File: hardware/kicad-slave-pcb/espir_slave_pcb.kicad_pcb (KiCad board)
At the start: 2 copper layers, 52 x 47 mm, 38 parts, among them Q2 AO3400A, Q4 AO3401A, SW1 RESET, SW2 BOOT, SW3 SS12D07VG6, U2 IR333C, U3 IR333C, U5 ESP32-C6-MINI-1, U6 AP2112K-3.3, U7 LiPo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

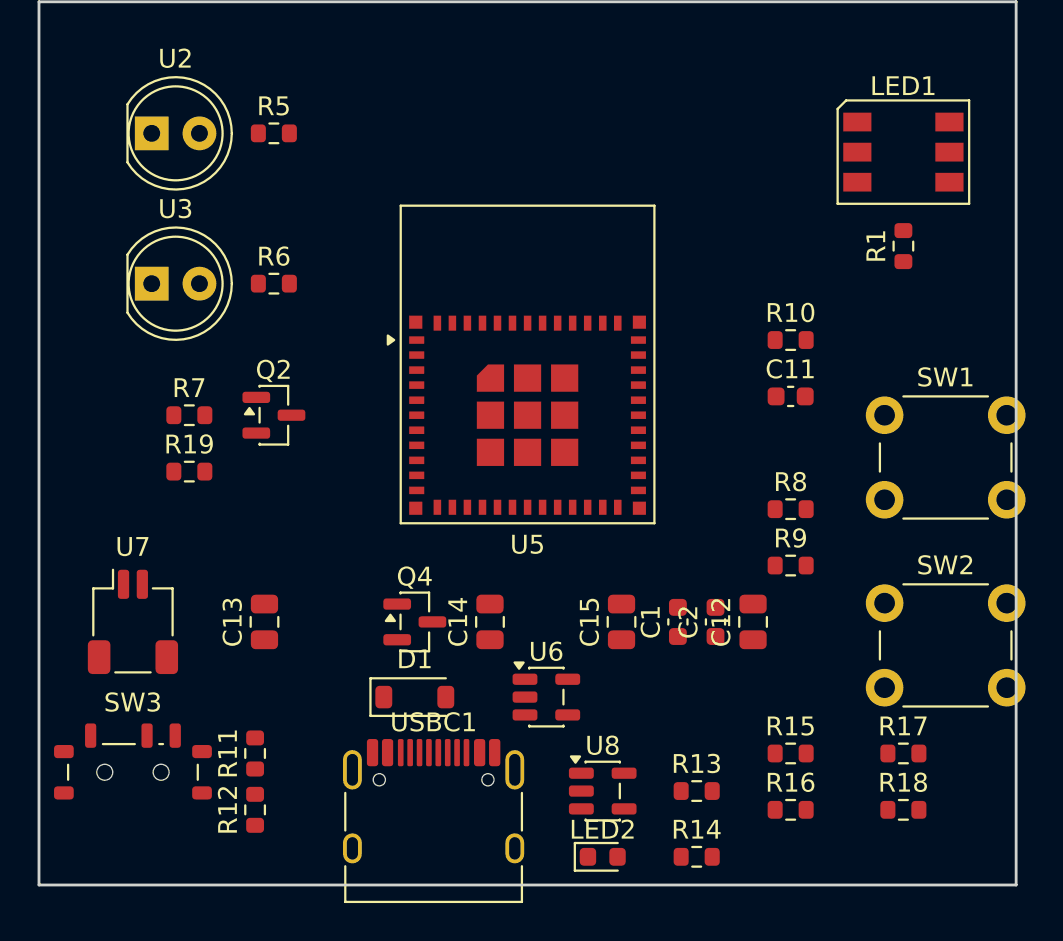
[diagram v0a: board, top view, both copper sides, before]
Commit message: hardware: autoroute the KiCad slave PCB (Freerouting)
Add net classes (Power 0.5mm, IR 0.4mm) in place_and_outline.py so the
current-carrying rails route wide, then autoroute headless via Freerouting
(route.sh: pcbnew ExportSpecctraDSN -> freerouting -> ImportSpecctraSES).

~90% routed (310 tracks, 26 vias): 104 of 114 connections. Carrying the net
classes into the DSN cut track_width DRC violations from 199 (uniform width)
to 8. The last 10 (IR-LED corner + WS2812 group) are too cramped to reach on
2 layers and, with the antenna-keepout / edge-clearance cleanup, are the GUI
finishing pass (4 layers would let it fully autoroute).
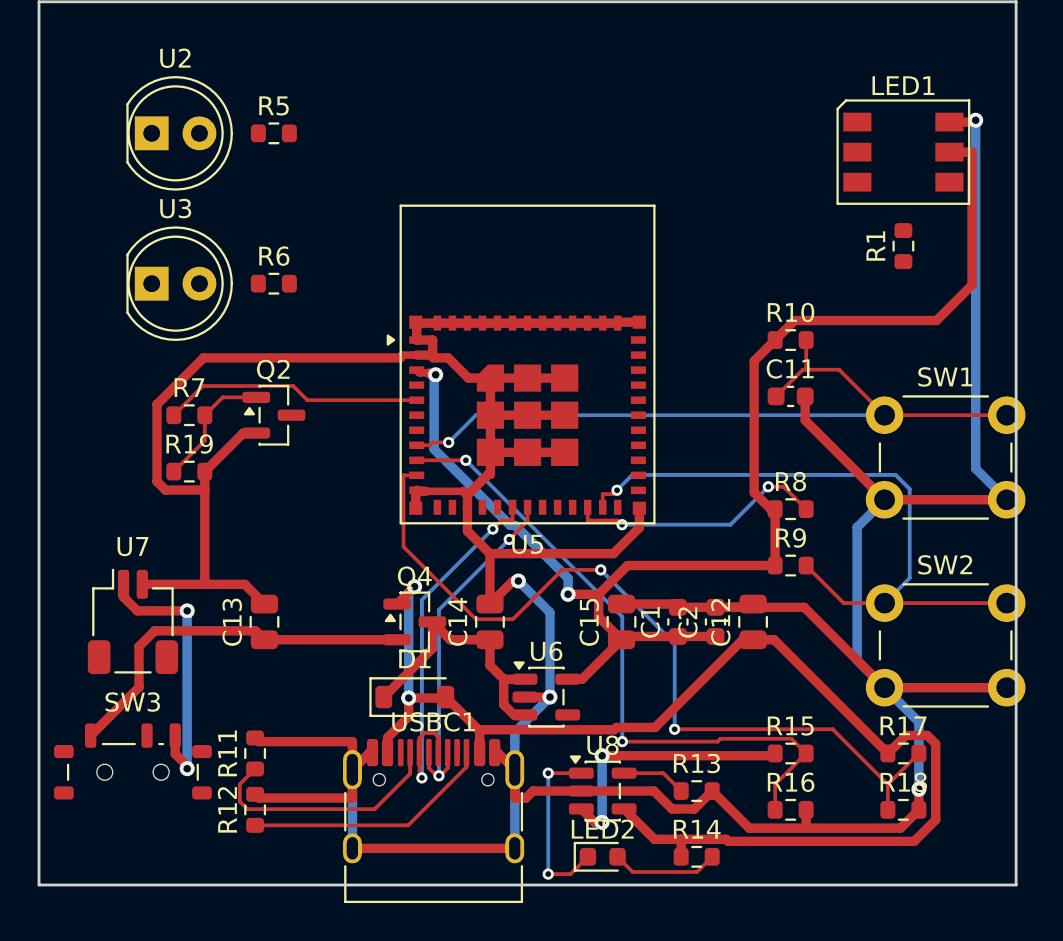
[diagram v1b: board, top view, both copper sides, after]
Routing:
- net GND: track 0.00 -> 248.1 mm, vias 0 -> 4
- net V3V3: track 0.00 -> 72.3 mm, vias 0 -> 2
- net V5: track 0.00 -> 68.6 mm, vias 0 -> 2
- net VBUS_SENSE: track 0.00 -> 44.0 mm, vias 0 -> 2
- net EN: track 0.00 -> 41.0 mm, vias 0 -> 1
- net BOOT: track 0.00 -> 35.9 mm, vias 0 -> 1
- net BATT_SENSE: track 0.00 -> 34.9 mm, vias 0 -> 2
- net VBAT: track 0.00 -> 34.3 mm, vias 0 -> 2
- net USB_DM: track 0.00 -> 20.9 mm, vias 0 -> 2
- net USB_DP: track 0.00 -> 19.3 mm, vias 0 -> 2
- net VCELL: track 0.00 -> 14.8 mm, vias 0 -> 2
- net VSYS: track 0.00 -> 14.8 mm
- net IR1: track 0.00 -> 13.9 mm
- net STRAP8: track 0.00 -> 13.7 mm, vias 0 -> 2
- net N$2: track 0.00 -> 13.3 mm
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
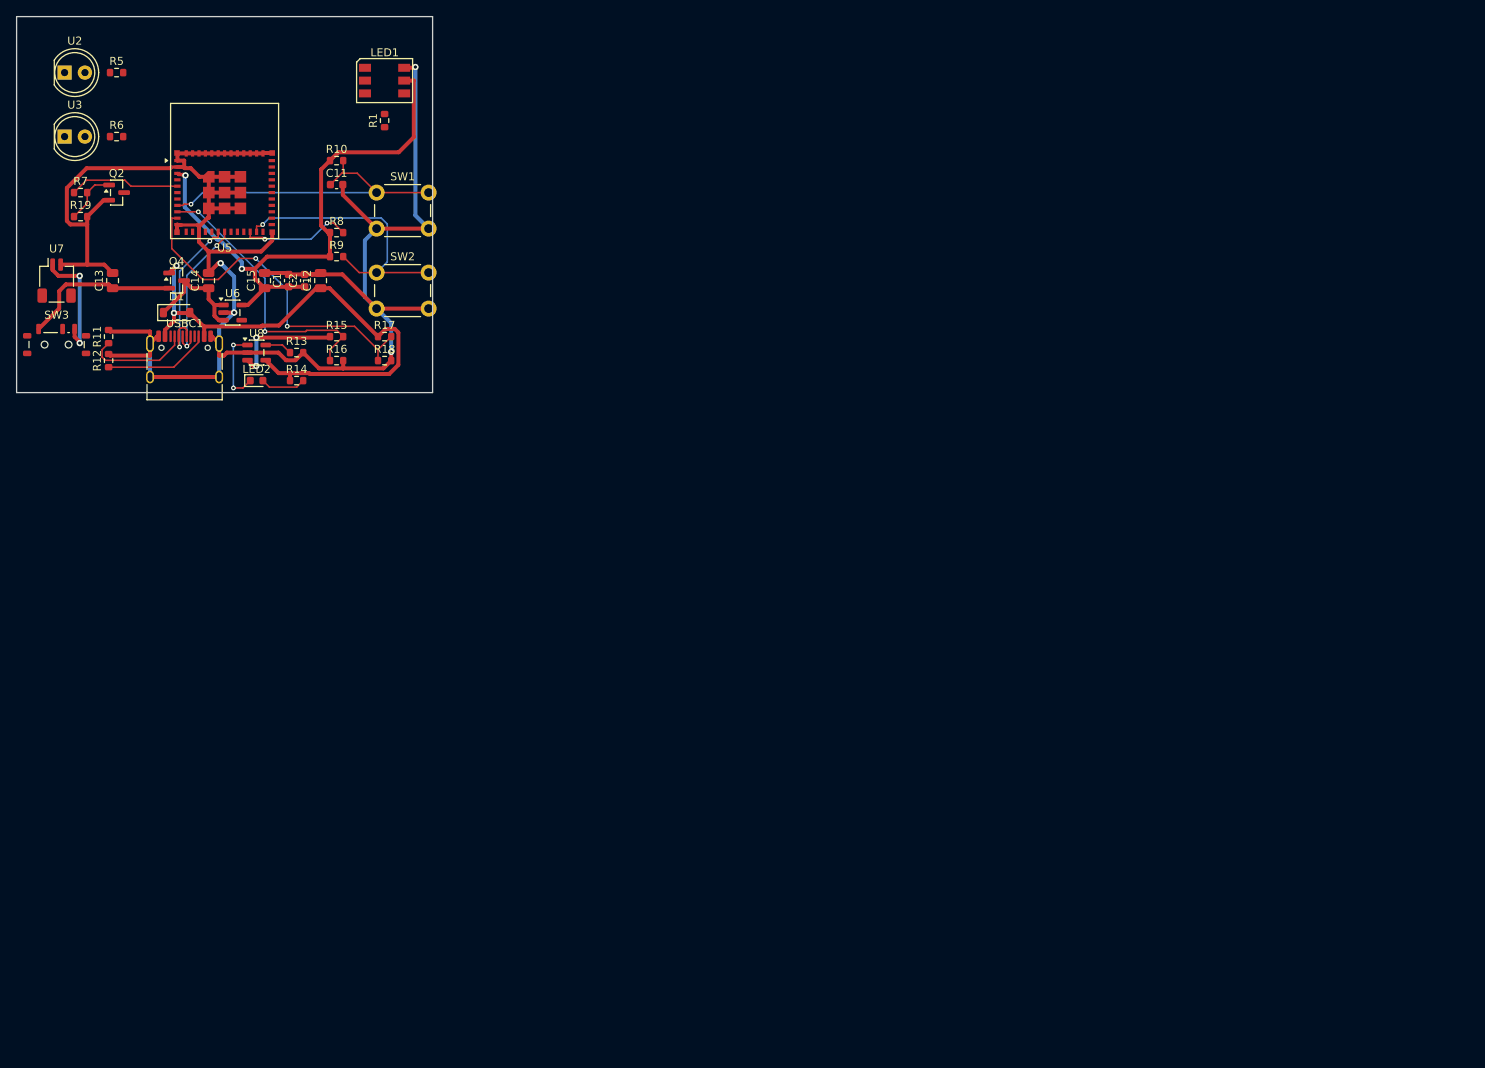
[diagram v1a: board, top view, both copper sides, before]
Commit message: hardware: fix module placement (antenna keep-out off-board) + centre on sheet
The ESP32-C6-MINI-1 footprint embeds a (keepout (tracks not_allowed)) antenna
zone (x±21.6, y[-26,-5.6]mm from origin). With the module in the board interior
that no-tracks band covered the IR LEDs (U2/U3) and WS2812 (LED1), making them
un-routable. Move the module so its body sits at the top edge and the antenna +
keep-out hang OFF the board: 19 keep-out DRC violations -> 0 and those nets now
route. Re-route lifts coverage ~90% -> ~98% (2 unrouted, 355 tracks, 25 vias).

Also offset placement + outline so the board is centred on the A4 sheet
(148.5, 105mm) instead of in the top-left corner. Previews regenerated.
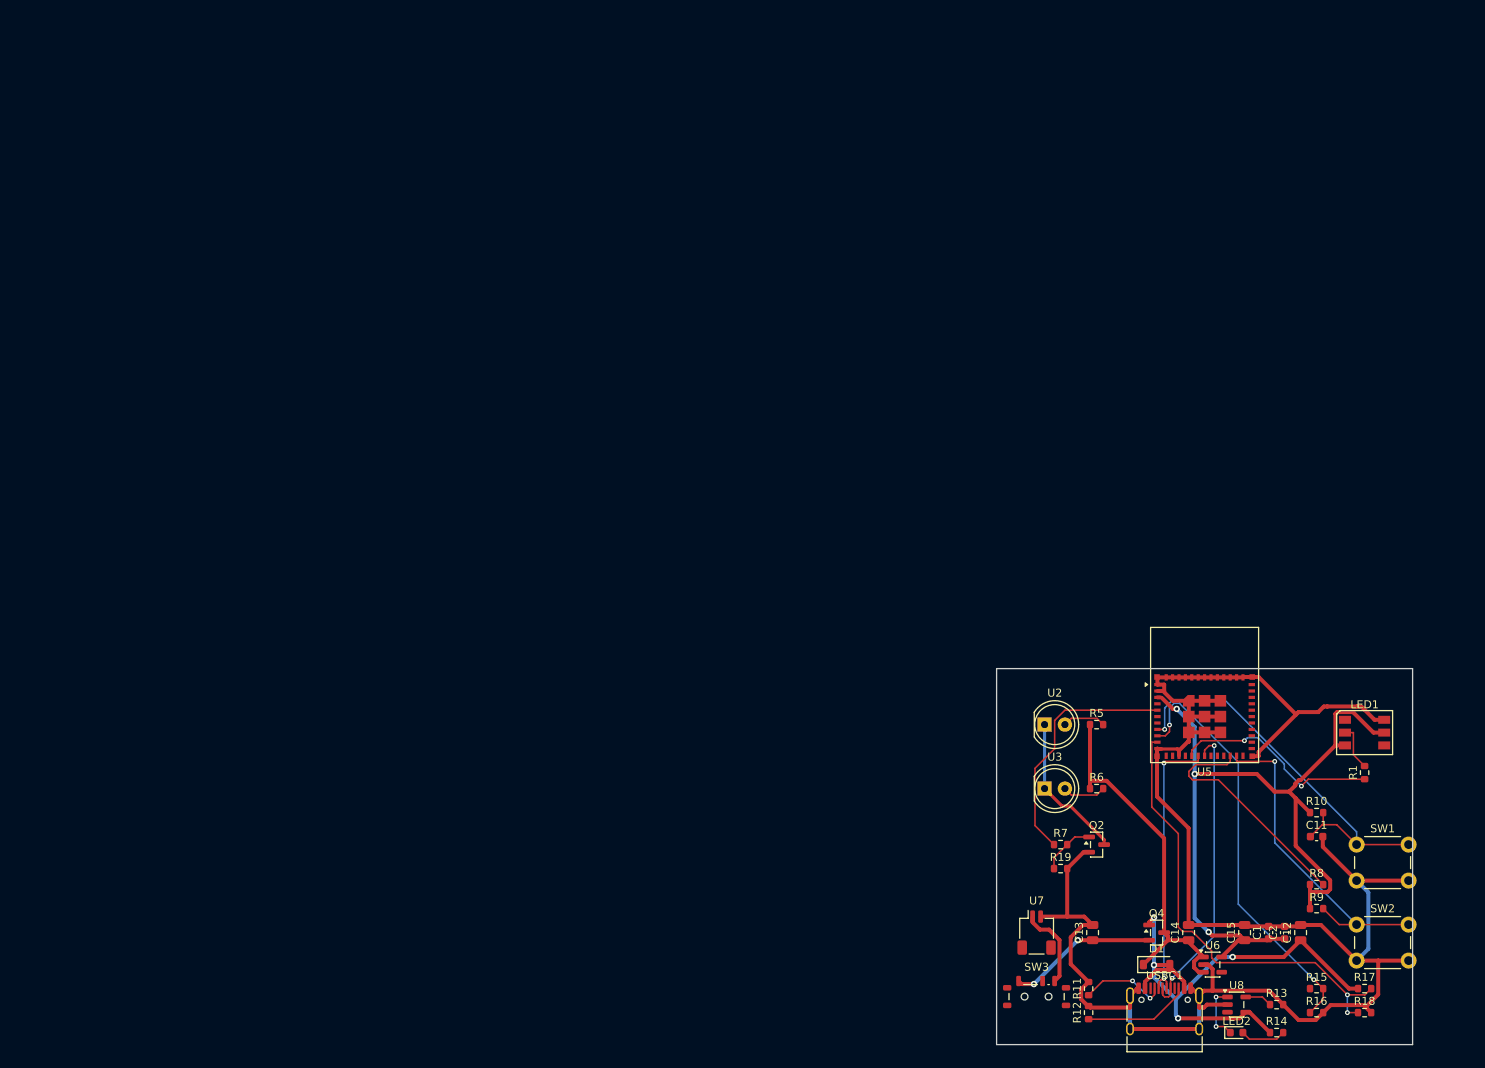
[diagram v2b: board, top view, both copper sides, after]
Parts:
- moved C1 147.1 mm to (156.5, 114.5)
- moved C11 147.1 mm to (162.5, 102.5)
- moved C12 147.1 mm to (160.5, 114.5)
- moved C13 147.1 mm to (134.5, 114.5)
- moved C14 147.1 mm to (146.5, 114.5)
- moved C15 147.1 mm to (153.5, 114.5)
- moved C2 147.1 mm to (158.5, 114.5)
- moved D1 147.1 mm to (142.5, 118.5)
- moved LED1 147.1 mm to (168.5, 89.5)
- moved LED2 147.1 mm to (152.5, 127.0)
- moved Q2 147.1 mm to (135.0, 103.5)
- moved Q4 147.1 mm to (142.5, 114.5)
- moved R1 147.1 mm to (168.5, 94.5)
- moved R10 147.1 mm to (162.5, 99.5)
- moved R11 147.1 mm to (134.0, 121.5)
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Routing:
- net VSYS: track 14.8 -> 46.4 mm
- net V3V3: track 72.3 -> 102.2 mm, vias 2 -> 3
- net WS_GPIO: track 0.00 -> 26.2 mm, vias 0 -> 2
- net IRD: track 0.00 -> 18.7 mm
- net USB_DP: track 19.3 -> 37.6 mm
- net BATT_SENSE: track 34.9 -> 53.0 mm
- net IR1: track 13.9 -> 30.9 mm
- net STRAP8: track 13.7 -> 29.4 mm, vias 2 -> 0
- net VBAT: track 34.3 -> 18.7 mm
- net USB_DM: track 20.9 -> 35.0 mm
- net VBUS_SENSE: track 44.0 -> 57.2 mm
- net EN: track 41.0 -> 51.9 mm
- net WS_DATA: track 0.00 -> 5.81 mm
- net BOOT: track 35.9 -> 41.6 mm
- net N$6: track 0.00 -> 5.45 mm
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
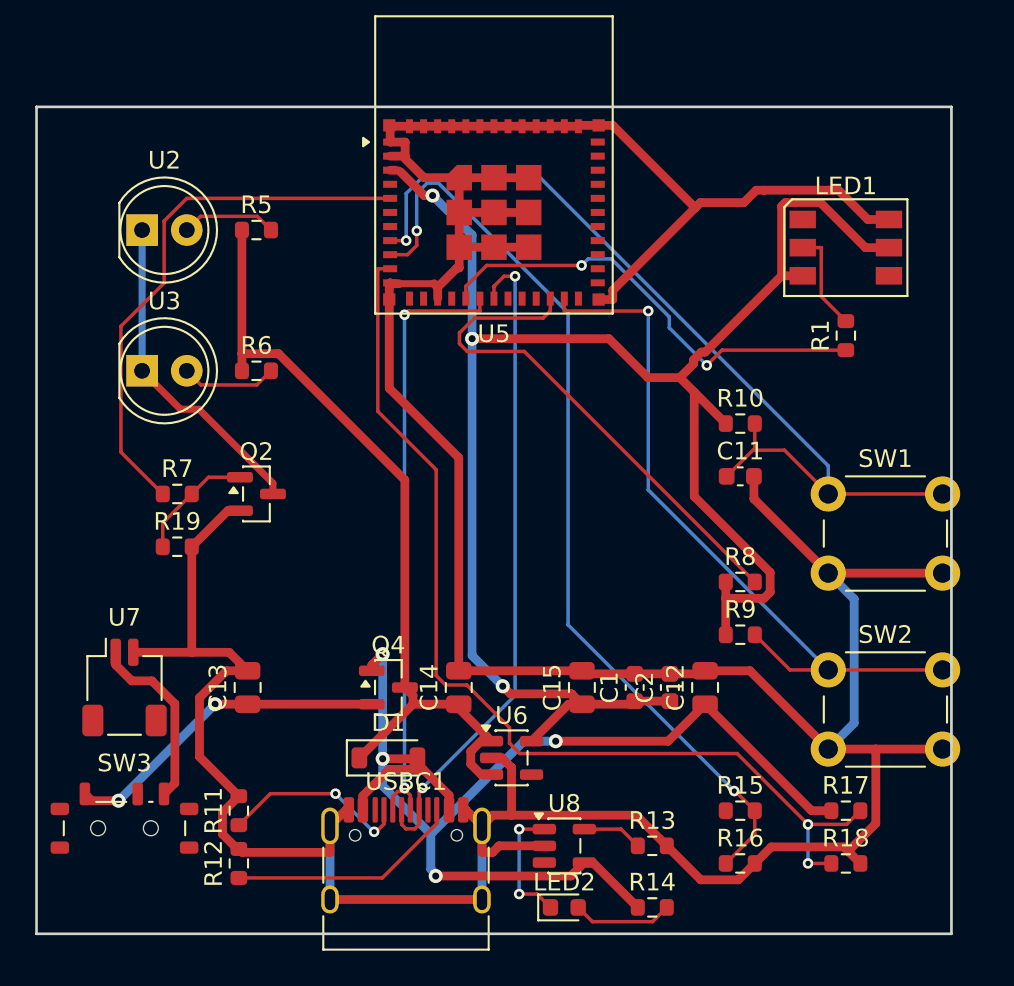
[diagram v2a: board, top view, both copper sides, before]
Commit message: hardware: DRC fixes — fully routed, wide power, clean except benign edge silk
Take DRC from 27 violations + 2 unrouted to 4 (all benign):
- Re-route to 0 unrouted (114/114; 540 tracks, 27 vias).
- Grow the right edge 1.5mm so SW1/SW2 pads + tracks clear it (8 copper_edge
  clearance -> 0).
- Main power rails widened to 0.5mm (track_width -> 0); VBAT kept at default in
  the congested charger corner (2-layer can't widen it there without clearance
  violations) — .kicad_dru updated to a VBAT-specific 0.2mm rule, rest 0.5mm.
- Delete zero-length track artifacts from the SES import.
- Silkscreen: collision-aware reposition of overlapping designators; hide LED2/
  USBC1 refs in the saturated cluster (still in BOM/CPL).

Remaining 4 = silk_edge_clearance on U5 antenna + USB-C outlines overhanging
their edges (by design; fab clips edge silk). 0 unconnected/track-width/
clearance/copper-edge.
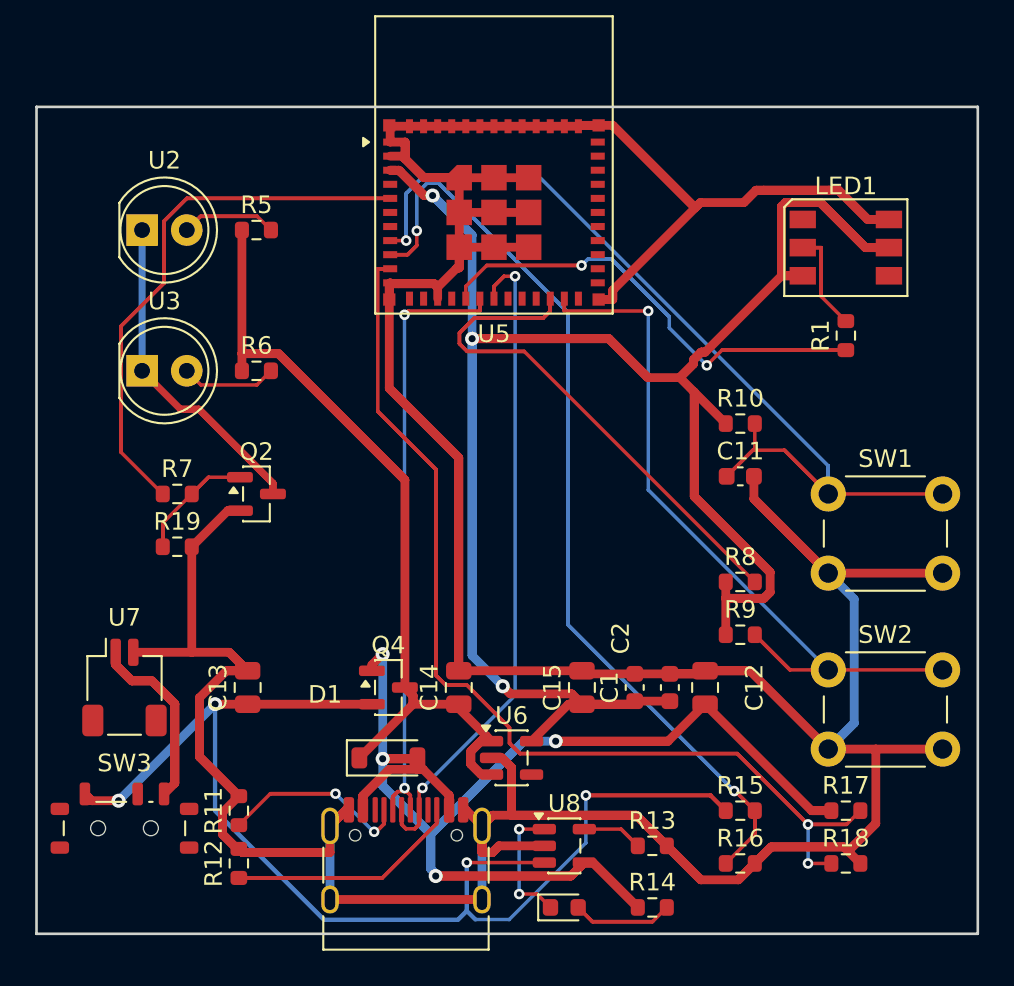
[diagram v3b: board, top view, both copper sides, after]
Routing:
- net GND: track 243.9 -> 351.8 mm
- net V3V3: track 102.2 -> 171.0 mm
- net VBAT: track 18.7 -> 69.4 mm, vias 2 -> 4
- net BATT_SENSE: track 53.0 -> 100.6 mm
- net VBUS_SENSE: track 57.2 -> 101.6 mm
- net V5: track 66.7 -> 106.3 mm
- net IR1: track 30.9 -> 58.4 mm
- net WS_GPIO: track 26.2 -> 45.1 mm
- net EN: track 51.9 -> 69.7 mm
- net VSYS: track 46.4 -> 62.5 mm
- net N$2: track 13.3 -> 25.8 mm
- net STRAP8: track 29.4 -> 40.2 mm
- net VCELL: track 10.4 -> 19.9 mm
- net IRD: track 18.7 -> 26.3 mm
- net N$1: track 10.9 -> 16.0 mm
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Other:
- board size 52 x 47 mm -> 53.5 x 47 mm
